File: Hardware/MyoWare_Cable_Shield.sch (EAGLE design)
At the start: 13 parts

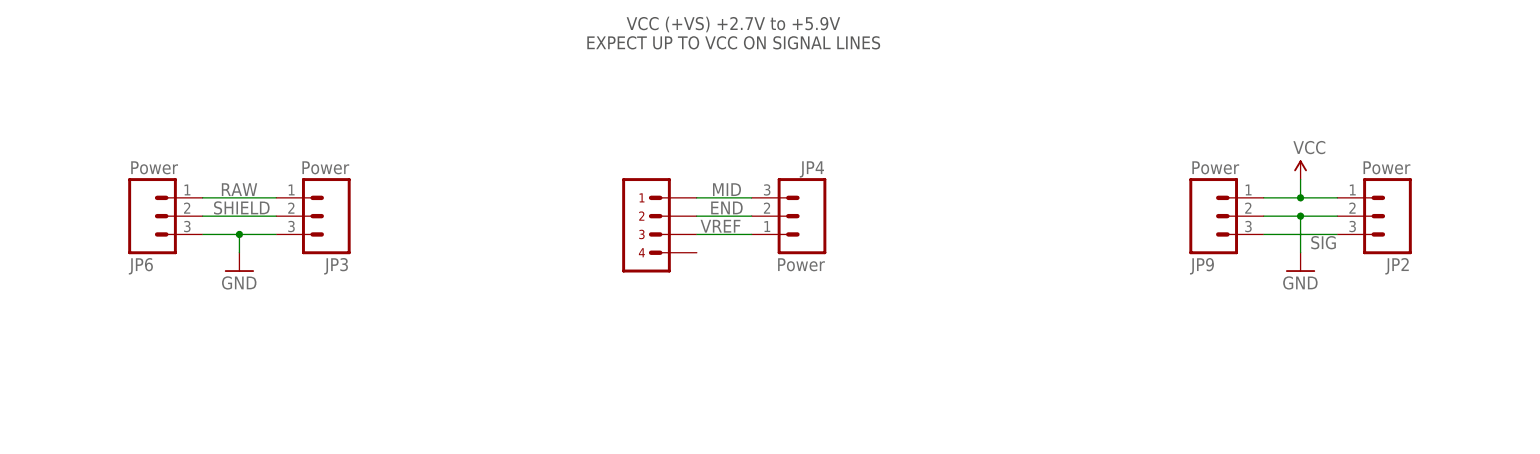
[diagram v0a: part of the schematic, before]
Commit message: changed audio jack to our common part
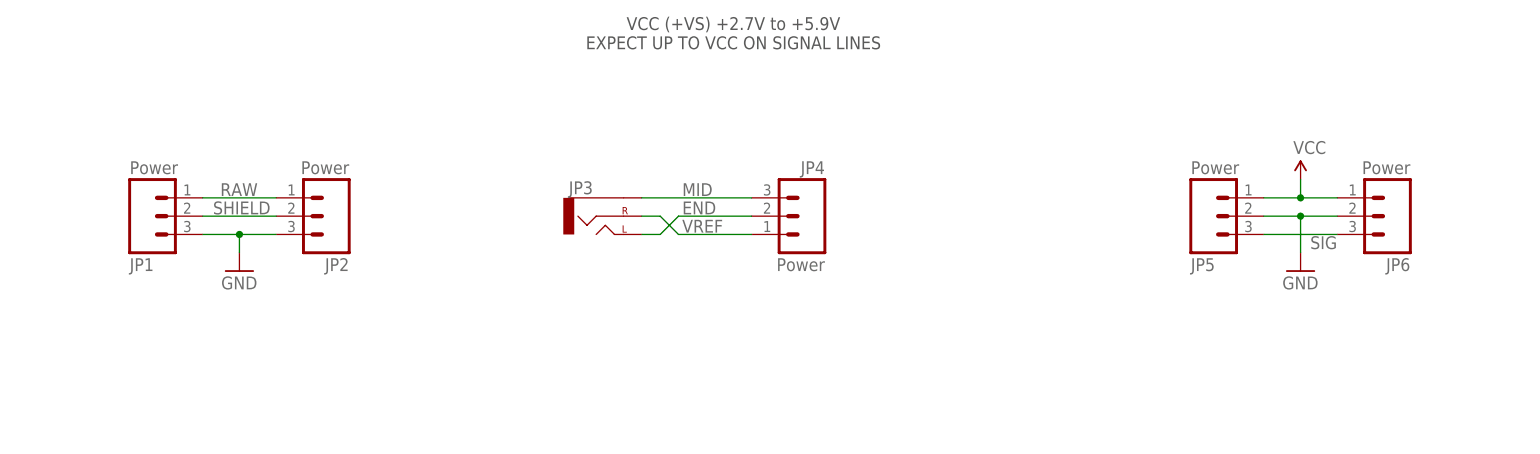
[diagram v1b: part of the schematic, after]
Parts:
- removed U$1: AUDIO_JACK, advancer-technologies:AUDIO_JACK
- added JP1: Power, SparkFun-Connectors:M031X03_NO_SILK
- JP3: value Power -> (none); device SparkFun-Connectors:M031X03_NO_SILK -> SparkFun-Connectors:AUDIO-JACKSMD2
- LOGO1: value OSHW-LOGOM -> SFE_LOGO_FLAME.2_INCH; device SparkFun-Aesthetics:OSHW-LOGOM -> SparkFun-Aesthetics:SFE_LOGO_FLAME.2_INCH
- LOGO2: value SFE_LOGO_FLAME.2_INCH -> OSHW-LOGOM; device SparkFun-Aesthetics:SFE_LOGO_FLAME.2_INCH -> SparkFun-Aesthetics:OSHW-LOGOM
- renumbered JP9 to JP5
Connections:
- net END: now also JP3.LEFT; no longer U$1.P$2
- net GND: now also JP1.3, JP2.3, JP6.2; no longer JP2.2, JP3.3, JP6.3
- net MID: now also JP3.SLEEVE; no longer U$1.P$1
- net RAW: now also JP1.1, JP2.1; no longer JP3.1, JP6.1
- net SHIELD: now also JP1.2, JP2.2; no longer JP3.2, JP6.2
- net SIG: now also JP6.3; no longer JP2.3
- net VCC: now also JP6.1; no longer JP2.1
- net VREF: now also JP3.RIGHT; no longer U$1.P$3
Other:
- moved on the sheet: JP2, JP3, JP6

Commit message: Bumped version number to 10 on sch
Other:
- note added: "v10"
- note removed: "v01"
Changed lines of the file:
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@@
 <?xml version="1.0" encoding="utf-8"?>
 <!DOCTYPE eagle SYSTEM "eagle.dtd">
-<eagle version="7.3.0">
+<eagle version="7.4.0">
 <drawing>
 <settings>
@@
 <text x="166.116" y="11.43" size="2.54" layer="94">Brian E Kaminski of Advancer Technologies</text>
 <text x="148.59" y="7.366" size="2.54" layer="94" ratio="10">Revised by: Brent Wilkins</text>
-<text x="236.22" y="7.62" size="2.54" layer="94" font="vector">v01</text>
+<text x="236.22" y="7.62" size="2.54" layer="94" font="vector">v10</text>
 <text x="116.84" y="114.3" size="1.778" layer="97" font="vector" ratio="15" align="center">VCC (+VS) +2.7V to +5.9V
 EXPECT UP TO VCC ON SIGNAL LINES</text>

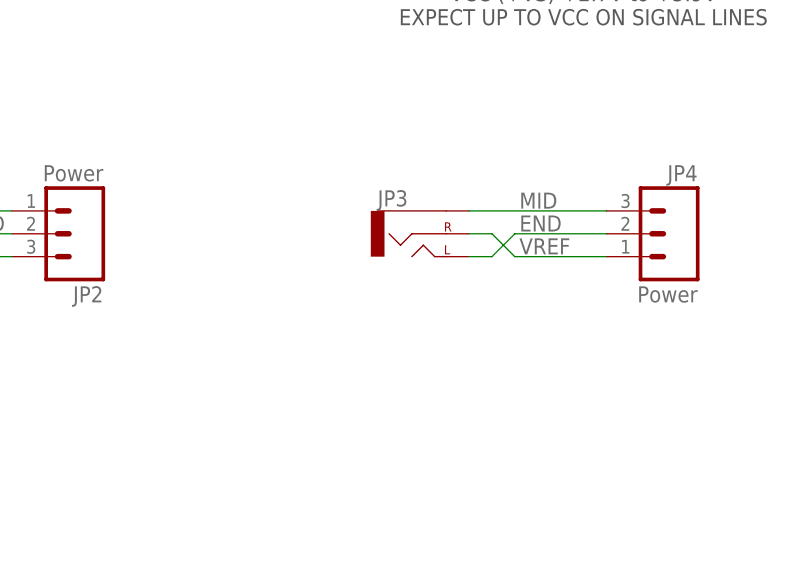
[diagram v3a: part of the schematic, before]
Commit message: Gave the jack a value of '3.5mm jack'
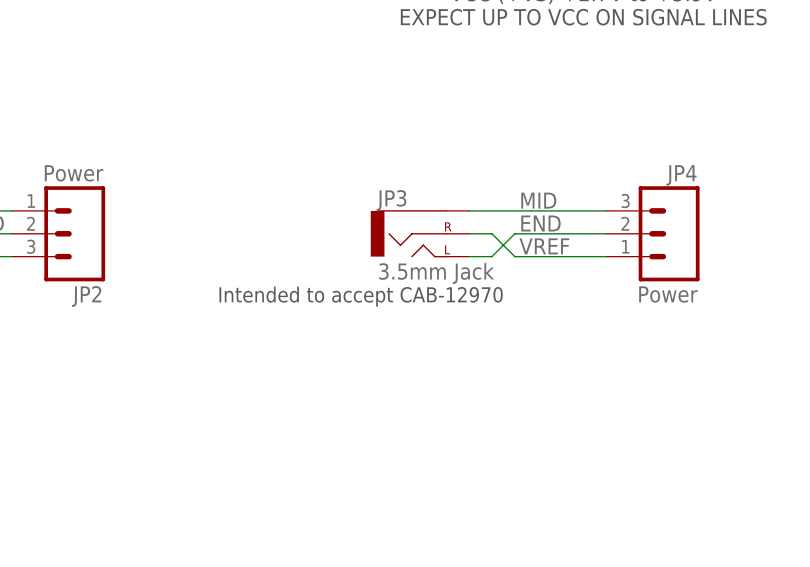
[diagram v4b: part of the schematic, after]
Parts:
- JP3: value (none) -> 3.5mm Jack
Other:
- note added: "Intended to accept CAB-12970"
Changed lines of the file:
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@@
 <part name="FID2" library="SparkFun-Aesthetics" deviceset="FIDUCIAL" device="1X2"/>
 <part name="FID1" library="SparkFun-Aesthetics" deviceset="FIDUCIAL" device="1X2"/>
-<part name="JP3" library="SparkFun-Connectors" deviceset="AUDIO-JACK" device="SMD2"/>
+<part name="JP3" library="SparkFun-Connectors" deviceset="AUDIO-JACK" device="SMD2" value="3.5mm Jack"/>
 </parts>
 <sheets>
@@
 <text x="116.84" y="114.3" size="1.778" layer="97" font="vector" ratio="15" align="center">VCC (+VS) +2.7V to +5.9V
 EXPECT UP TO VCC ON SIGNAL LINES</text>
+<text x="76.2" y="81.28" size="1.6764" layer="97" font="vector" ratio="15">Intended to accept CAB-12970</text>
 </plain>
 <instances>

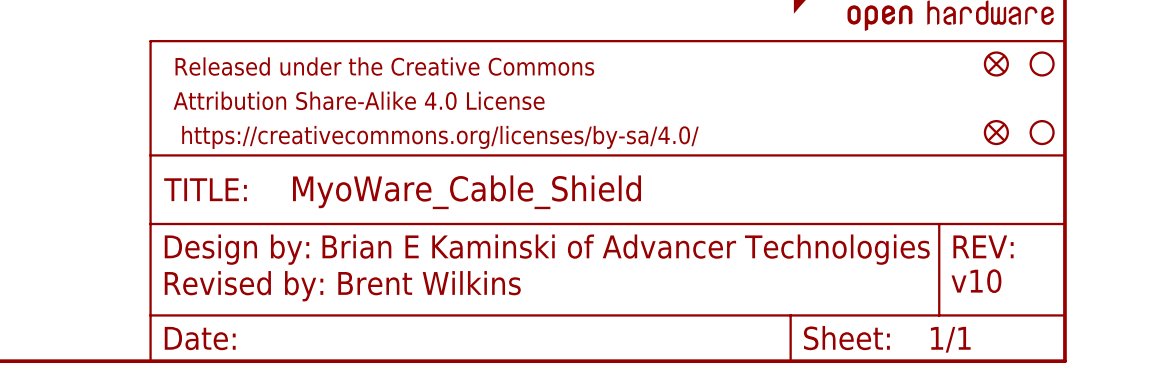
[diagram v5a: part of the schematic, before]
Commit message: V11
REM Headers Lining Up
Traces Adjusted
Board Origin Fix
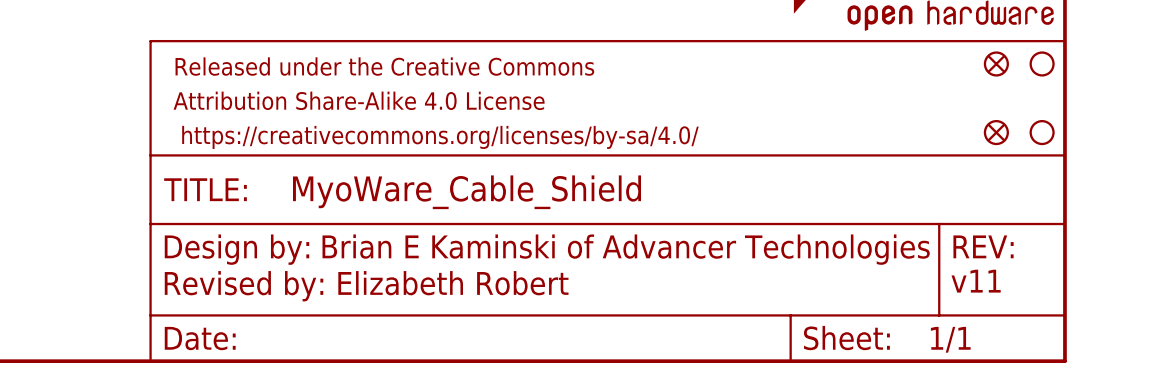
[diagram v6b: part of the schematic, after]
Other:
- note added: "Revised by: Elizabeth Robert"
- note added: "v11"
- note removed: "Revised by: Brent Wilkins"
- note removed: "v10"
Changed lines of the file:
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@@
 <?xml version="1.0" encoding="utf-8"?>
 <!DOCTYPE eagle SYSTEM "eagle.dtd">
-<eagle version="7.4.0">
+<eagle version="7.7.0">
 <drawing>
 <settings>
@@
 <plain>
 <text x="166.116" y="11.43" size="2.54" layer="94">Brian E Kaminski of Advancer Technologies</text>
-<text x="148.59" y="7.366" size="2.54" layer="94" ratio="10">Revised by: Brent Wilkins</text>
-<text x="236.22" y="7.62" size="2.54" layer="94" font="vector">v10</text>
+<text x="148.59" y="7.366" size="2.54" layer="94" ratio="10">Revised by: Elizabeth Robert</text>
+<text x="236.22" y="7.62" size="2.54" layer="94" font="vector">v11</text>
 <text x="116.84" y="114.3" size="1.778" layer="97" font="vector" ratio="15" align="center">VCC (+VS) +2.7V to +5.9V
 EXPECT UP TO VCC ON SIGNAL LINES</text>

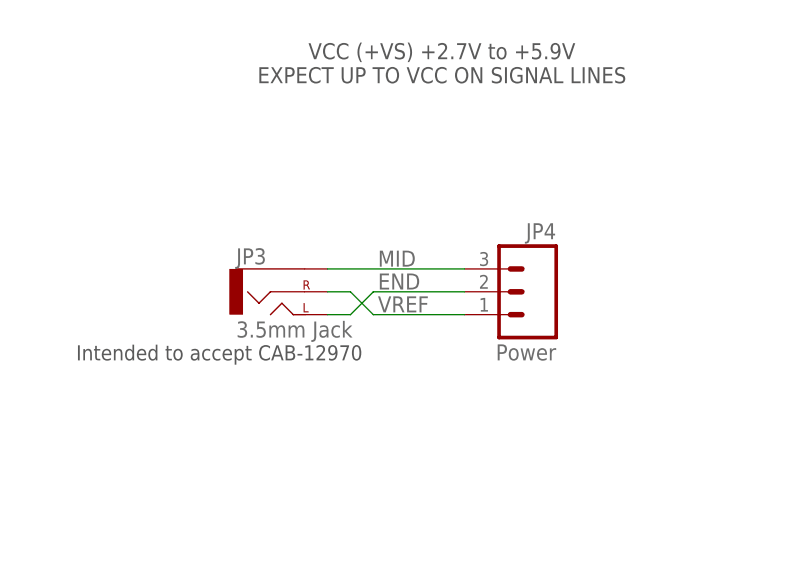
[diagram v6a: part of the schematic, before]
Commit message: Rewiring of 3.5mm Jack
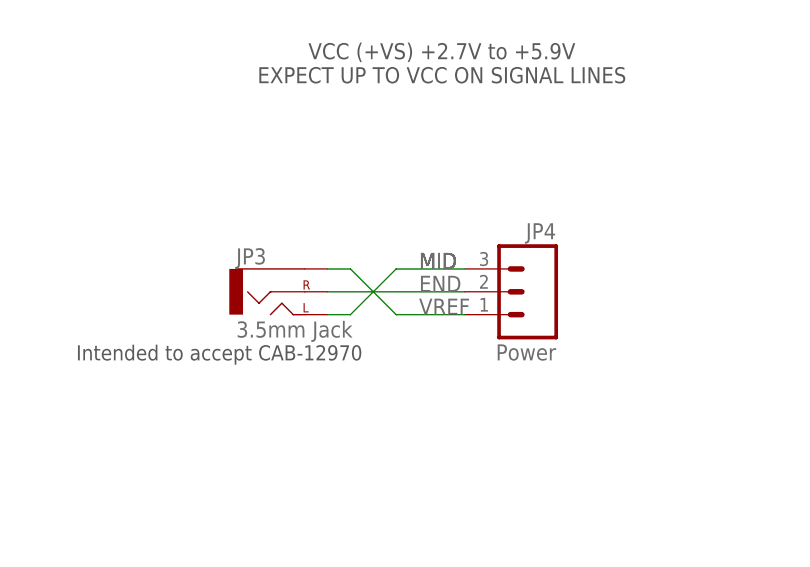
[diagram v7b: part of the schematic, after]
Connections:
- net END: now also JP3.RIGHT; no longer JP3.LEFT
- net MID: now also JP3.LEFT; no longer JP3.SLEEVE
- net VREF: now also JP3.SLEEVE; no longer JP3.RIGHT
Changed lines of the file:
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@@
 </busses>
 <nets>
-<net name="MID" class="0">
-<segment>
-<pinref part="JP4" gate="G$1" pin="3"/>
-<label x="109.728" y="91.694" size="1.778" layer="95"/>
-<wire x1="104.14" y1="91.44" x2="119.38" y2="91.44" width="0.1524" layer="91"/>
-<pinref part="JP3" gate="G$1" pin="SLEEVE"/>
-</segment>
-</net>
-<net name="END" class="0">
-<segment>
-<pinref part="JP4" gate="G$1" pin="2"/>
-<label x="109.728" y="89.154" size="1.778" layer="95"/>
-<wire x1="109.22" y1="88.9" x2="119.38" y2="88.9" width="0.1524" layer="91"/>
-<pinref part="JP3" gate="G$1" pin="LEFT"/>
-<wire x1="104.14" y1="86.36" x2="106.68" y2="86.36" width="0.1524" layer="91"/>
-<wire x1="106.68" y1="86.36" x2="109.22" y2="88.9" width="0.1524" layer="91"/>
-</segment>
-</net>
-<net name="VREF" class="0">
-<segment>
-<pinref part="JP4" gate="G$1" pin="1"/>
-<label x="109.728" y="86.614" size="1.778" layer="95"/>
-<wire x1="109.22" y1="86.36" x2="119.38" y2="86.36" width="0.1524" layer="91"/>
-<pinref part="JP3" gate="G$1" pin="RIGHT"/>
-<wire x1="104.14" y1="88.9" x2="106.68" y2="88.9" width="0.1524" layer="91"/>
-<wire x1="106.68" y1="88.9" x2="109.22" y2="86.36" width="0.1524" layer="91"/>
-</segment>
-</net>
 <net name="SHIELD" class="0">
 <segment>
@@
 </segment>
 </net>
+<net name="MID" class="0">
+<segment>
+<pinref part="JP4" gate="G$1" pin="3"/>
+<wire x1="119.38" y1="91.44" x2="111.76" y2="91.44" width="0.1524" layer="91"/>
+<wire x1="111.76" y1="91.44" x2="106.68" y2="86.36" width="0.1524" layer="91"/>
+<pinref part="JP3" gate="G$1" pin="LEFT"/>
+<wire x1="106.68" y1="86.36" x2="104.14" y2="86.36" width="0.1524" layer="91"/>
+<label x="114.3" y="91.44" size="1.778" layer="95"/>
+<label x="114.3" y="91.44" size="1.778" layer="95"/>
+<label x="114.3" y="91.44" size="1.778" layer="95"/>
+</segment>
+</net>
+<net name="VREF" class="0">
+<segment>
+<pinref part="JP3" gate="G$1" pin="SLEEVE"/>
+<wire x1="104.14" y1="91.44" x2="106.68" y2="91.44" width="0.1524" layer="91"/>
+<wire x1="106.68" y1="91.44" x2="111.76" y2="86.36" width="0.1524" layer="91"/>
+<pinref part="JP4" gate="G$1" pin="1"/>
+<wire x1="111.76" y1="86.36" x2="119.38" y2="86.36" width="0.1524" layer="91"/>
+<label x="114.3" y="86.36" size="1.778" layer="95"/>
+</segment>
+</net>
+<net name="END" class="0">
+<segment>
+<pinref part="JP4" gate="G$1" pin="2"/>
+<pinref part="JP3" gate="G$1" pin="RIGHT"/>
+<wire x1="119.38" y1="88.9" x2="104.14" y2="88.9" width="0.1524" layer="91"/>
+<label x="114.3" y="88.9" size="1.778" layer="95"/>
+</segment>
+</net>

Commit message: Revert "V11"
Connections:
- net END: now also JP3.LEFT; no longer JP3.RIGHT
- net MID: now also JP3.SLEEVE; no longer JP3.LEFT
- net VREF: now also JP3.RIGHT; no longer JP3.SLEEVE
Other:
- note added: "Revised by: Brent Wilkins"
- note added: "v10"
- note removed: "Revised by: Elizabeth Robert"
- note removed: "v11"
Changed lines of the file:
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@@
 <?xml version="1.0" encoding="utf-8"?>
 <!DOCTYPE eagle SYSTEM "eagle.dtd">
-<eagle version="7.7.0">
+<eagle version="7.4.0">
 <drawing>
 <settings>
@@
 <plain>
 <text x="166.116" y="11.43" size="2.54" layer="94">Brian E Kaminski of Advancer Technologies</text>
-<text x="148.59" y="7.366" size="2.54" layer="94" ratio="10">Revised by: Elizabeth Robert</text>
-<text x="236.22" y="7.62" size="2.54" layer="94" font="vector">v11</text>
+<text x="148.59" y="7.366" size="2.54" layer="94" ratio="10">Revised by: Brent Wilkins</text>
+<text x="236.22" y="7.62" size="2.54" layer="94" font="vector">v10</text>
 <text x="116.84" y="114.3" size="1.778" layer="97" font="vector" ratio="15" align="center">VCC (+VS) +2.7V to +5.9V
 EXPECT UP TO VCC ON SIGNAL LINES</text>
@@
 </busses>
 <nets>
+<net name="MID" class="0">
+<segment>
+<pinref part="JP4" gate="G$1" pin="3"/>
+<label x="109.728" y="91.694" size="1.778" layer="95"/>
+<wire x1="104.14" y1="91.44" x2="119.38" y2="91.44" width="0.1524" layer="91"/>
+<pinref part="JP3" gate="G$1" pin="SLEEVE"/>
+</segment>
+</net>
+<net name="END" class="0">
+<segment>
+<pinref part="JP4" gate="G$1" pin="2"/>
+<label x="109.728" y="89.154" size="1.778" layer="95"/>
+<wire x1="109.22" y1="88.9" x2="119.38" y2="88.9" width="0.1524" layer="91"/>
+<pinref part="JP3" gate="G$1" pin="LEFT"/>
+<wire x1="104.14" y1="86.36" x2="106.68" y2="86.36" width="0.1524" layer="91"/>
+<wire x1="106.68" y1="86.36" x2="109.22" y2="88.9" width="0.1524" layer="91"/>
+</segment>
+</net>
+<net name="VREF" class="0">
+<segment>
+<pinref part="JP4" gate="G$1" pin="1"/>
+<label x="109.728" y="86.614" size="1.778" layer="95"/>
+<wire x1="109.22" y1="86.36" x2="119.38" y2="86.36" width="0.1524" layer="91"/>
+<pinref part="JP3" gate="G$1" pin="RIGHT"/>
+<wire x1="104.14" y1="88.9" x2="106.68" y2="88.9" width="0.1524" layer="91"/>
+<wire x1="106.68" y1="88.9" x2="109.22" y2="86.36" width="0.1524" layer="91"/>
+</segment>
+</net>
 <net name="SHIELD" class="0">
 <segment>
@@
 </segment>
 </net>
-<net name="MID" class="0">
-<segment>
-<pinref part="JP4" gate="G$1" pin="3"/>
-<wire x1="119.38" y1="91.44" x2="111.76" y2="91.44" width="0.1524" layer="91"/>
-<wire x1="111.76" y1="91.44" x2="106.68" y2="86.36" width="0.1524" layer="91"/>
-<pinref part="JP3" gate="G$1" pin="LEFT"/>
-<wire x1="106.68" y1="86.36" x2="104.14" y2="86.36" width="0.1524" layer="91"/>
-<label x="114.3" y="91.44" size="1.778" layer="95"/>
-<label x="114.3" y="91.44" size="1.778" layer="95"/>
-<label x="114.3" y="91.44" size="1.778" layer="95"/>
-</segment>
-</net>
-<net name="VREF" class="0">
-<segment>
-<pinref part="JP3" gate="G$1" pin="SLEEVE"/>
-<wire x1="104.14" y1="91.44" x2="106.68" y2="91.44" width="0.1524" layer="91"/>
-<wire x1="106.68" y1="91.44" x2="111.76" y2="86.36" width="0.1524" layer="91"/>
-<pinref part="JP4" gate="G$1" pin="1"/>
-<wire x1="111.76" y1="86.36" x2="119.38" y2="86.36" width="0.1524" layer="91"/>
-<label x="114.3" y="86.36" size="1.778" layer="95"/>
-</segment>
-</net>
-<net name="END" class="0">
-<segment>
-<pinref part="JP4" gate="G$1" pin="2"/>
-<pinref part="JP3" gate="G$1" pin="RIGHT"/>
-<wire x1="119.38" y1="88.9" x2="104.14" y2="88.9" width="0.1524" layer="91"/>
-<label x="114.3" y="88.9" size="1.778" layer="95"/>
-</segment>
-</net>
